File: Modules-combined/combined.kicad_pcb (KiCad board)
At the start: 2 copper layers, 100 x 100 mm, 245 parts

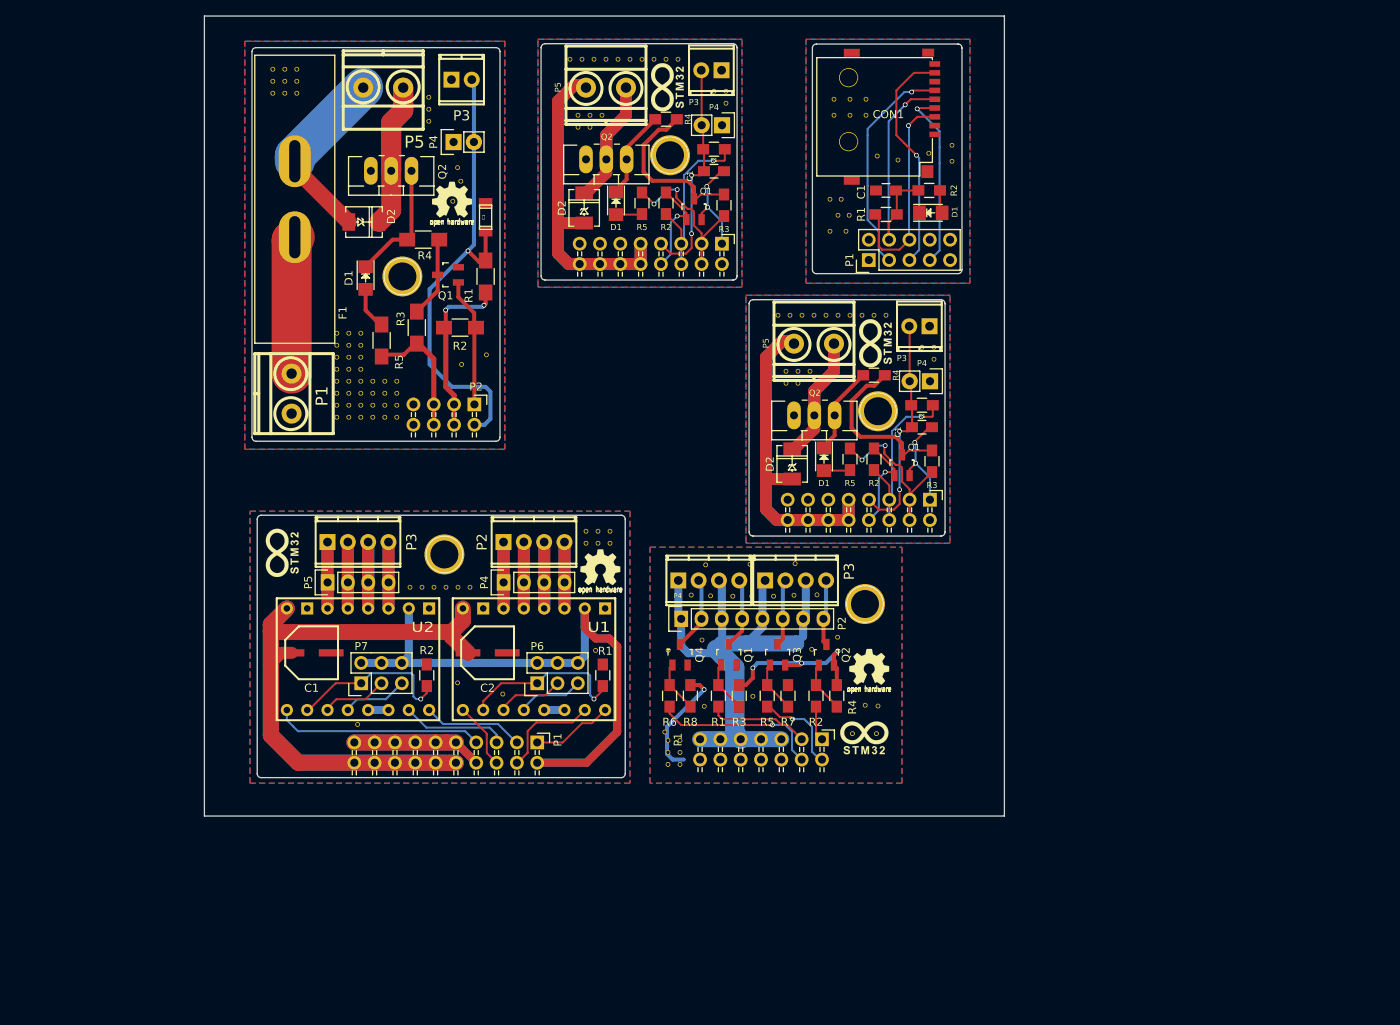
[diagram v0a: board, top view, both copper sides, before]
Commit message: Finished Combined PCB and Gerber files
Combined pcb fits on 10x10cm, breakable and gerbers are finished for elecrow order. will order everything this weekend, lets see if it works.
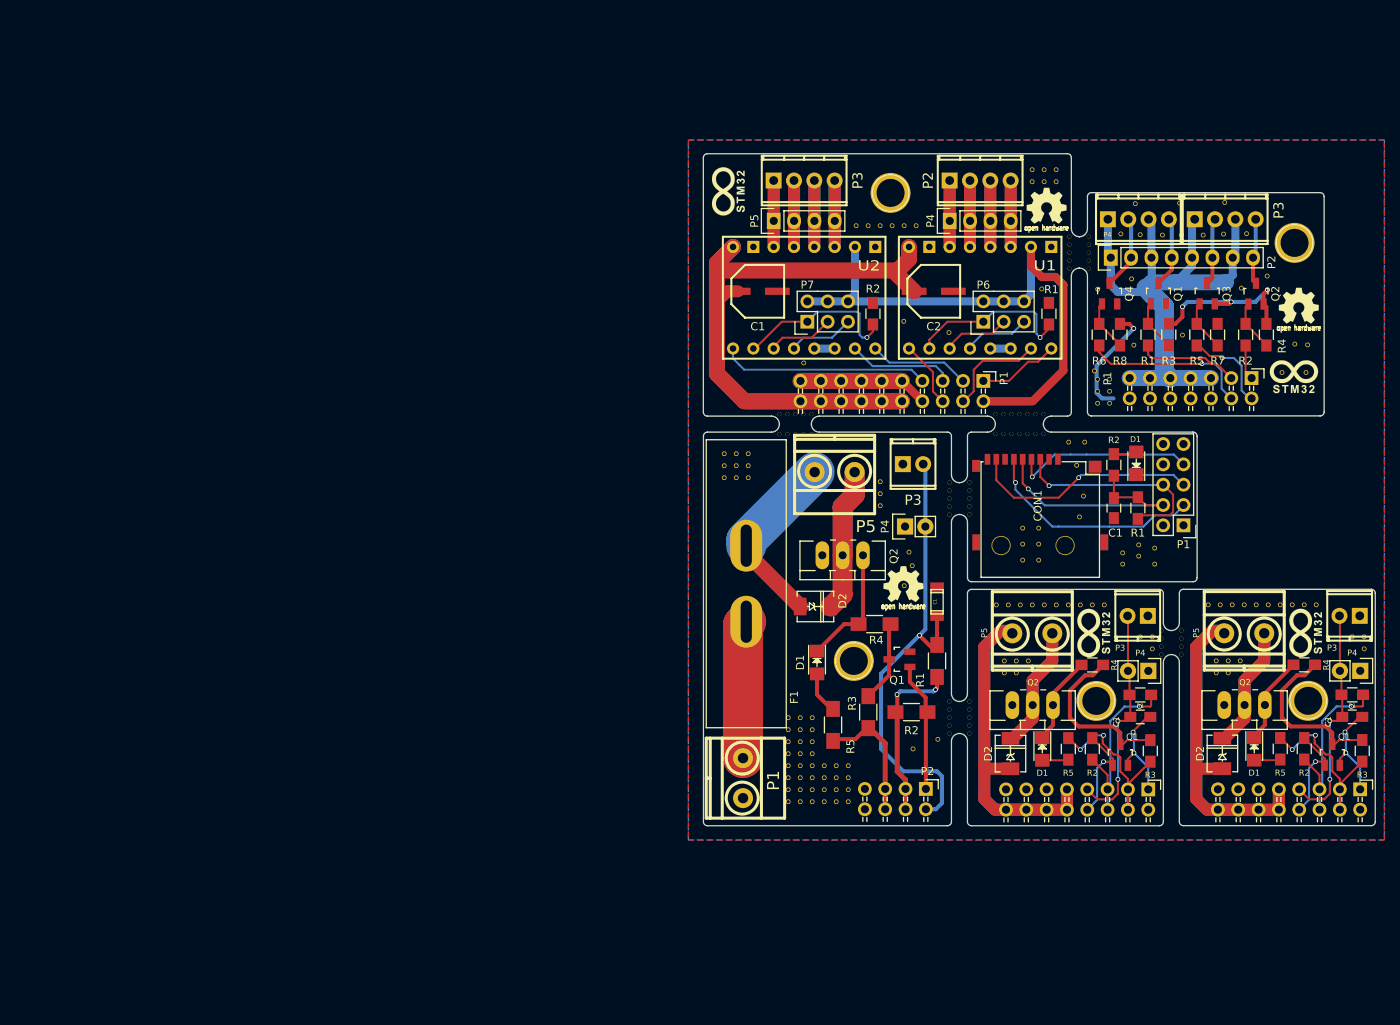
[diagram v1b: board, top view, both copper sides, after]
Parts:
- removed the ? at (189.0, 67.5)
- removed the ? at (189.0, 66.0)
- removed the ? at (187.5, 66.0)
- removed the ? at (172.0, 70.5)
- removed the ? at (170.5, 70.5)
- removed the ? at (173.5, 69.0)
- removed the ? at (172.0, 69.0)
- removed the ? at (170.5, 69.0)
- removed the ? at (183.0, 62.0)
- removed the ? at (181.5, 62.0)
- removed the ? at (180.0, 62.0)
- removed the ? at (178.5, 62.0)
- removed the ? at (177.0, 62.0)
- removed the ? at (175.5, 62.0)
- removed the ? at (174.0, 62.0)
- removed the ? at (172.5, 62.0)
- removed the ? at (171.0, 62.0)
- removed the ? at (181.4, 67.7)
- removed the ? at (181.8, 65.5)
- removed the ? at (182.0, 74.0)
- removed the ? at (169.5, 62.0)
- removed the ? at (146.0, 38.5)
- removed the ? at (144.5, 38.5)
- removed the ? at (147.5, 37.0)
- removed the ? at (146.0, 37.0)
- removed the ? at (144.5, 37.0)
- removed the ? at (151.0, 30.0)
- removed the ? at (149.5, 30.0)
- removed the ? at (148.0, 30.0)
- removed the ? at (146.5, 30.0)
- removed the ? at (145.0, 30.0)
- removed the ? at (143.5, 30.0)
- removed the ? at (163.0, 35.5)
- removed the ? at (163.0, 34.0)
- removed the ? at (161.5, 34.0)
- removed the ? at (157.0, 30.0)
- removed the ? at (155.5, 30.0)
- removed the ? at (154.0, 30.0)
- removed the ? at (152.5, 30.0)
- removed the ? at (155.4, 35.7)
- removed the ? at (155.8, 33.5)
- removed the ? at (156.0, 42.0)
- removed the C1 at (161.5, 44.0)
- removed the C1 at (187.5, 76.0)
- removed the D1 at (149.2, 48.0)
- removed the D1 at (175.2, 80.0)
- removed the D2 at (145.3, 48.6)
- removed the D2 at (171.3, 80.6)
- removed the P1 at (162.5, 53.1)
- removed the P1 at (188.5, 85.1)
- removed the P3 at (161.2, 31.4)
- removed the P3 at (187.2, 63.4)
- removed the P4 at (162.5, 38.2)
- removed the P4 at (188.5, 70.2)
- removed the P5 at (148.0, 33.5)
- removed the P5 at (174.0, 65.5)
- removed the Q1 at (159.0, 48.8)
- removed the Q1 at (185.0, 80.8)
- removed the Q2 at (148.0, 42.5)
- removed the Q2 at (174.0, 74.5)
- removed the R1 at (161.5, 41.2)
- removed the R1 at (187.5, 73.2)
- removed the R2 at (155.5, 48.0)
- removed the R2 at (181.5, 80.0)
- removed the R3 at (162.8, 48.2)
- removed the R3 at (188.8, 80.2)
- removed the R4 at (155.5, 37.5)
- removed the R4 at (181.5, 69.5)
- removed the R5 at (152.5, 48.0)
- removed the R5 at (178.5, 80.0)
- added ?: , ReST-Library:VIA-0.6mm, F.Cu at (202.8, 98.2)
- added ?: , ReST-Library:VIA-0.6mm, F.Cu at (201.3, 98.2)
- added ?: , ReST-Library:VIA-0.6mm, F.Cu at (199.8, 98.2)
- added ?: , ReST-Library:VIA-0.6mm, F.Cu at (198.3, 98.2)
- added ?: , ReST-Library:Logo_silk_OSHW_6x6mm, B.Cu at (208.7, 103.9)
- added ?: , ReST-Library:STM32, F.Cu at (209.0, 101.7)
- added ?: , Connect:1pin, F.Cu at (209.3, 110.2)
- added ?: , ReST-Library:VIA-0.6mm, F.Cu at (196.8, 98.2)
- added ?: , ReST-Library:VIA-0.6mm, F.Cu at (242.8, 103.7)
- added ?: , ReST-Library:VIA-0.6mm, F.Cu at (242.8, 102.2)
- added ?: , ReST-Library:VIA-0.6mm, F.Cu at (241.3, 102.2)
- added ?: , ReST-Library:VIA-0.6mm, F.Cu at (225.8, 106.7)
- added ?: , ReST-Library:VIA-0.6mm, F.Cu at (224.3, 106.7)
- added ?: , ReST-Library:VIA-0.6mm, F.Cu at (227.3, 105.2)
- added ?: , ReST-Library:VIA-0.6mm, F.Cu at (225.8, 105.2)
- added ?: , ReST-Library:VIA-0.6mm, F.Cu at (224.3, 105.2)
- added ?: , ReST-Library:VIA-0.6mm, F.Cu at (236.8, 98.2)
- added ?: , ReST-Library:VIA-0.6mm, F.Cu at (235.3, 98.2)
- added ?: , ReST-Library:VIA-0.6mm, F.Cu at (233.8, 98.2)
- added ?: , ReST-Library:VIA-0.6mm, F.Cu at (232.3, 98.2)
- added ?: , ReST-Library:VIA-0.6mm, F.Cu at (230.8, 98.2)
- added ?: , ReST-Library:VIA-0.6mm, F.Cu at (229.3, 98.2)
- added ?: , ReST-Library:VIA-0.6mm, F.Cu at (227.8, 98.2)
- added ?: , ReST-Library:VIA-0.6mm, F.Cu at (226.3, 98.2)
- added ?: , ReST-Library:VIA-0.6mm, F.Cu at (224.8, 98.2)
- added ?: , ReST-Library:Logo_silk_OSHW_6x6mm, B.Cu at (235.2, 103.9)
- added ?: , ReST-Library:STM32, F.Cu at (235.5, 101.7)
- added ?: , Connect:1pin, F.Cu at (235.8, 110.2)
- added ?: , ReST-Library:VIA-0.6mm, F.Cu at (223.3, 98.2)
- added ?: , ReST-Library:VIA-0.6mm, F.Cu at (216.3, 103.7)
- added ?: , ReST-Library:VIA-0.6mm, F.Cu at (216.3, 102.2)
- added ?: , ReST-Library:VIA-0.6mm, F.Cu at (214.8, 102.2)
- added ?: , ReST-Library:VIA-0.6mm, F.Cu at (199.3, 106.7)
- added ?: , ReST-Library:VIA-0.6mm, F.Cu at (197.8, 106.7)
- added ?: , ReST-Library:VIA-0.6mm, F.Cu at (200.8, 105.2)
- added ?: , ReST-Library:VIA-0.6mm, F.Cu at (199.3, 105.2)
- added ?: , ReST-Library:VIA-0.6mm, F.Cu at (197.8, 105.2)
- added ?: , ReST-Library:VIA-0.6mm, F.Cu at (210.3, 98.2)
- added ?: , ReST-Library:VIA-0.6mm, F.Cu at (208.8, 98.2)
- added ?: , ReST-Library:VIA-0.6mm, F.Cu at (207.3, 98.2)
- added ?: , ReST-Library:VIA-0.6mm, F.Cu at (205.8, 98.2)
- added ?: , ReST-Library:VIA-0.6mm, F.Cu at (204.3, 98.2)
- added C1: , Capacitors_SMD:C_0805_HandSoldering, F.Cu at (214.8, 112.2)
- added C1: , Capacitors_SMD:C_0805_HandSoldering, F.Cu at (241.3, 112.2)
- added D1: , LEDs:LED_1206, F.Cu at (202.5, 116.2)
- added D1: , LEDs:LED_1206, F.Cu at (229.0, 116.2)
- added D2: , ReST-Library:DO-214AC(SMA), F.Cu at (198.6, 116.8)
- added D2: , ReST-Library:DO-214AC(SMA), F.Cu at (225.1, 116.8)
- added P1: , ReST-Library:Pin_Header_Angled_2x08, F.Cu at (215.8, 121.3)
- added P1: , ReST-Library:Pin_Header_Angled_2x08, F.Cu at (242.3, 121.3)
- added P3: , ReST-Library:screw-2,54-2P, F.Cu at (214.5, 99.6)
- added P3: , ReST-Library:screw-2,54-2P, F.Cu at (241.0, 99.6)
- added P4: , Pin_Headers:Pin_Header_Straight_1x02, F.Cu at (215.8, 106.5)
- added P4: , Pin_Headers:Pin_Header_Straight_1x02, F.Cu at (242.3, 106.5)
- added P5: , ReST-Library:screw-5-2P, F.Cu at (201.3, 101.8)
- added P5: , ReST-Library:screw-5-2P, F.Cu at (227.8, 101.8)
- added Q1: , ReST-Library:SOT-23, F.Cu at (212.3, 117.0)
- added Q1: , ReST-Library:SOT-23, F.Cu at (238.8, 117.0)
- added Q2: , TO_SOT_Packages_THT:TO-220_Neutral123_Vertical_LargePads, F.Cu at (201.3, 110.7)
- added Q2: , TO_SOT_Packages_THT:TO-220_Neutral123_Vertical_LargePads, F.Cu at (227.8, 110.7)
- added R1: , Resistors_SMD:R_0805_HandSoldering, F.Cu at (214.8, 109.5)
- added R1: , Resistors_SMD:R_0805_HandSoldering, F.Cu at (241.3, 109.5)
- added R2: , Resistors_SMD:R_0805_HandSoldering, F.Cu at (208.8, 116.2)
- added R2: , Resistors_SMD:R_0805_HandSoldering, F.Cu at (235.3, 116.2)
- added R3: , Resistors_SMD:R_0805_HandSoldering, F.Cu at (216.0, 116.5)
- added R3: , Resistors_SMD:R_0805_HandSoldering, F.Cu at (242.5, 116.5)
- added R4: , Resistors_SMD:R_0805_HandSoldering, F.Cu at (208.8, 105.7)
- added R4: , Resistors_SMD:R_0805_HandSoldering, F.Cu at (235.3, 105.7)
- added R5: , Resistors_SMD:R_0805_HandSoldering, F.Cu at (205.8, 116.2)
- added R5: , Resistors_SMD:R_0805_HandSoldering, F.Cu at (232.3, 116.2)
- added REF**11: , ReST-Library:VIA-0.6mm, F.Cu at (169.7, 74.4)
- added REF**111: , ReST-Library:VIA-0.6mm, F.Cu at (169.7, 76.9)
- added REF**11111: , ReST-Library:VIA-0.6mm, F.Cu at (196.7, 74.4)
- added REF**111111: , ReST-Library:VIA-0.6mm, F.Cu at (190.9, 82.9)
- added REF**111111: , ReST-Library:VIA-0.6mm, F.Cu at (196.7, 76.8)
- added REF**11111111: , ReST-Library:VIA-0.6mm, F.Cu at (205.9, 52.2)
- added REF**111111111: , ReST-Library:VIA-0.6mm, F.Cu at (193.4, 82.9)
- added REF**111111111: , ReST-Library:VIA-0.6mm, F.Cu at (208.3, 52.2)
- added REF**1111111111: , ReST-Library:VIA-0.6mm, F.Cu at (190.9, 110.3)
- added REF**11111111111: , ReST-Library:VIA-0.6mm, F.Cu at (193.4, 110.3)
- added REF**1111111111111: , ReST-Library:VIA-0.6mm, F.Cu at (217.4, 101.4)
- added REF**11111111111111: , ReST-Library:VIA-0.6mm, F.Cu at (219.9, 101.4)
- added REF**11111111111112: , ReST-Library:VIA-0.6mm, F.Cu at (219.9, 102.4)
- added REF**11111111111113: , ReST-Library:VIA-0.6mm, F.Cu at (219.9, 103.4)
- added REF**11111111111114: , ReST-Library:VIA-0.6mm, F.Cu at (219.9, 104.4)
- added REF**1111111111112: , ReST-Library:VIA-0.6mm, F.Cu at (217.4, 102.4)
- added REF**1111111111113: , ReST-Library:VIA-0.6mm, F.Cu at (217.4, 103.4)
- added REF**1111111111114: , ReST-Library:VIA-0.6mm, F.Cu at (217.4, 104.4)
- added REF**11111111112: , ReST-Library:VIA-0.6mm, F.Cu at (193.4, 111.3)
- added REF**11111111113: , ReST-Library:VIA-0.6mm, F.Cu at (193.4, 112.3)
- added REF**11111111114: , ReST-Library:VIA-0.6mm, F.Cu at (193.4, 113.3)
- added REF**11111111115: , ReST-Library:VIA-0.6mm, F.Cu at (193.4, 114.3)
- added REF**1111111112: , ReST-Library:VIA-0.6mm, F.Cu at (190.9, 111.3)
- added REF**1111111113: , ReST-Library:VIA-0.6mm, F.Cu at (190.9, 112.3)
- added REF**1111111114: , ReST-Library:VIA-0.6mm, F.Cu at (190.9, 113.3)
- added REF**1111111115: , ReST-Library:VIA-0.6mm, F.Cu at (190.9, 114.3)
- added REF**111111112: , ReST-Library:VIA-0.6mm, F.Cu at (193.4, 83.9)
- added REF**111111112: , ReST-Library:VIA-0.6mm, F.Cu at (208.3, 53.2)
- added REF**111111113: , ReST-Library:VIA-0.6mm, F.Cu at (193.4, 84.9)
- added REF**111111113: , ReST-Library:VIA-0.6mm, F.Cu at (208.3, 54.2)
- added REF**111111114: , ReST-Library:VIA-0.6mm, F.Cu at (193.4, 85.9)
- added REF**111111114: , ReST-Library:VIA-0.6mm, F.Cu at (208.3, 55.2)
- added REF**111111115: , ReST-Library:VIA-0.6mm, F.Cu at (193.4, 86.9)
- added REF**111111115: , ReST-Library:VIA-0.6mm, F.Cu at (208.3, 56.2)
- added REF**11111112: , ReST-Library:VIA-0.6mm, F.Cu at (205.9, 53.2)
- added REF**11111113: , ReST-Library:VIA-0.6mm, F.Cu at (205.9, 54.2)
- added REF**11111114: , ReST-Library:VIA-0.6mm, F.Cu at (205.9, 55.2)
- added REF**11111115: , ReST-Library:VIA-0.6mm, F.Cu at (205.9, 56.2)
- added REF**111112: , ReST-Library:VIA-0.6mm, F.Cu at (190.9, 83.9)
- added REF**111113: , ReST-Library:VIA-0.6mm, F.Cu at (190.9, 84.9)
- added REF**111114: , ReST-Library:VIA-0.6mm, F.Cu at (190.9, 85.9)
- added REF**111115: , ReST-Library:VIA-0.6mm, F.Cu at (190.9, 86.9)
- added REF**111121: , ReST-Library:VIA-0.6mm, F.Cu at (197.7, 76.8)
- added REF**111131: , ReST-Library:VIA-0.6mm, F.Cu at (198.7, 76.8)
- added REF**111141: , ReST-Library:VIA-0.6mm, F.Cu at (199.7, 76.8)
- added REF**111151: , ReST-Library:VIA-0.6mm, F.Cu at (200.7, 76.8)
- added REF**111161: , ReST-Library:VIA-0.6mm, F.Cu at (201.7, 76.8)
- added REF**111171: , ReST-Library:VIA-0.6mm, F.Cu at (202.7, 76.8)
- added REF**11121: , ReST-Library:VIA-0.6mm, F.Cu at (197.7, 74.4)
- added REF**11131: , ReST-Library:VIA-0.6mm, F.Cu at (198.7, 74.4)
- added REF**11141: , ReST-Library:VIA-0.6mm, F.Cu at (199.7, 74.4)
- added REF**11151: , ReST-Library:VIA-0.6mm, F.Cu at (200.7, 74.4)
- added REF**11161: , ReST-Library:VIA-0.6mm, F.Cu at (201.7, 74.4)
- added REF**11171: , ReST-Library:VIA-0.6mm, F.Cu at (202.7, 74.4)
- added REF**121: , ReST-Library:VIA-0.6mm, F.Cu at (170.7, 76.9)
- added REF**131: , ReST-Library:VIA-0.6mm, F.Cu at (171.7, 76.9)
- added REF**141: , ReST-Library:VIA-0.6mm, F.Cu at (172.7, 76.9)
- added REF**151: , ReST-Library:VIA-0.6mm, F.Cu at (173.7, 76.9)
- added REF**21: , ReST-Library:VIA-0.6mm, F.Cu at (170.7, 74.4)
- added REF**31: , ReST-Library:VIA-0.6mm, F.Cu at (171.7, 74.4)
- added REF**41: , ReST-Library:VIA-0.6mm, F.Cu at (172.7, 74.4)
- added REF**51: , ReST-Library:VIA-0.6mm, F.Cu at (173.7, 74.4)
- moved ? 74.1 mm to (186.4, 116.2)
- moved ? 74.1 mm to (189.5, 115.0)
- moved ? 74.1 mm to (178.3, 122.8)
- moved ? 74.1 mm to (176.8, 122.8)
- moved ? 74.1 mm to (175.3, 122.8)
- moved ? 74.1 mm to (178.3, 121.3)
- moved ? 74.1 mm to (176.8, 121.3)
- moved ? 74.1 mm to (175.3, 121.3)
- moved ? 74.1 mm to (178.3, 119.8)
- moved ? 74.1 mm to (176.8, 119.8)
- moved ? 74.1 mm to (175.3, 119.8)
- moved ? 74.1 mm to (178.3, 118.3)
- moved ? 74.1 mm to (176.8, 118.3)
- moved ? 74.1 mm to (175.3, 118.3)
- moved ? 74.1 mm to (185.3, 95.8)
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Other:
- board size 100 x 100 mm -> 84 x 84 mm
- rule pad_to_mask_clearance: 0 -> 0.2

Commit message: minor changes to values of components and footprints. added two leds for both 12V Rails.
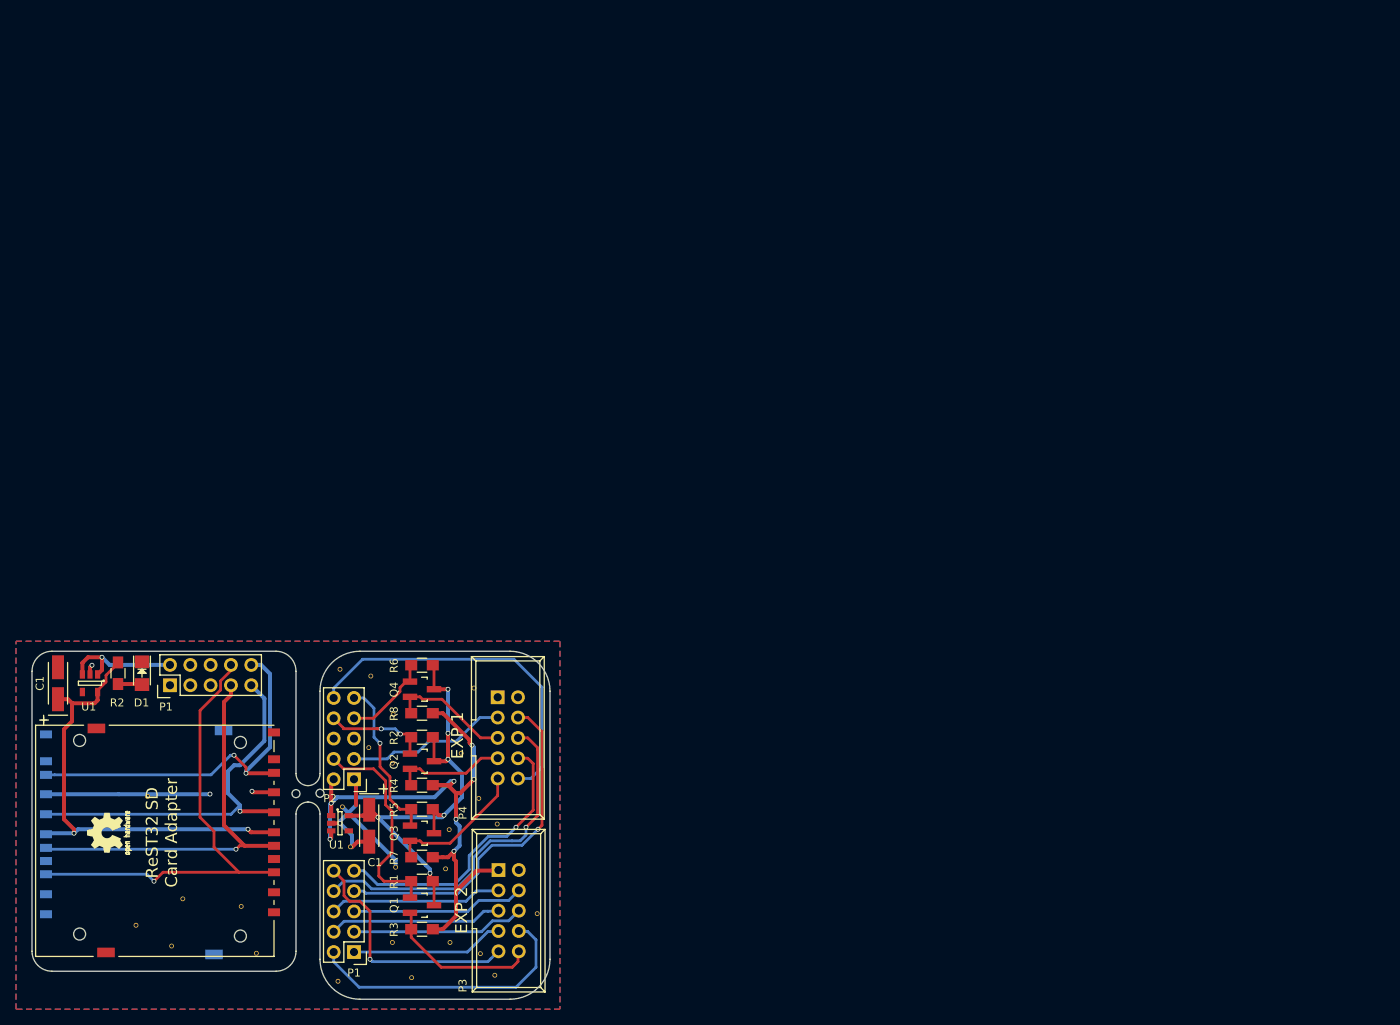
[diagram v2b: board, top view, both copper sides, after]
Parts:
- removed ? (x149), REF**11, REF**111, REF**11111, REF**111111 (x2), REF**11111111, REF**111111111 (x2), REF**1111111111, REF**11111111111, REF**1111111111111, REF**11111111111111, REF**11111111111112, REF**11111111111113, REF**11111111111114, REF**1111111111112, REF**1111111111113, REF**1111111111114, REF**11111111112, REF**11111111113, REF**11111111114, REF**11111111115, REF**1111111112, REF**1111111113, REF**1111111114, REF**1111111115, REF**111111112 (x2), REF**111111113 (x2), REF**111111114 (x2), REF**111111115 (x2), REF**11111112, REF**11111113, REF**11111114, REF**11111115, REF**111112, REF**111113, REF**111114, REF**111115, REF**111121, REF**111131, REF**111141, REF**111151, REF**111161, REF**111171, REF**11121, REF**11131, REF**11141, REF**11151, REF**11161, REF**11171, REF**121, REF**131, REF**141, REF**151, REF**21, REF**31, REF**41, REF**51: , ReST-Library:VIA-0.6mm
- removed ? (x6): , ReST-Library:Logo_silk_OSHW_6x6mm
- removed ? (x4): , ReST-Library:STM32
- removed ? (x5): , Connect:1pin
- removed ? (x2): , ReST-Library:STM32-6mm
- removed the C1 at (189.4, 97.8)
- removed the C1 at (214.8, 112.2)
- removed the C1 at (211.5, 86.1)
- removed the C1 at (241.3, 112.2)
- removed the C1 at (167.0, 59.0)
- removed C2: , ReST-Library:CP-PANASONIC-SMT_D8
- removed the D1 at (174.4, 105.4)
- removed the D1 at (202.5, 116.2)
- removed the D1 at (214.3, 80.5)
- removed the D1 at (229.0, 116.2)
- removed D2: , DO-214AC(SMA):DO-214AC(SMA)
- removed D2 (x2): , ReST-Library:DO-214AC(SMA)
- removed F1: , ReST-Librar:JEF-703C
- removed the P1 at (228.7, 69.9)
- removed the P1 at (165.1, 119.9)
- removed the P1 at (215.8, 121.3)
- removed the P1 at (220.2, 88.3)
- removed the P1 at (242.3, 121.3)
- removed the P1 at (195.2, 70.2)
- removed the P2 at (211.1, 54.8)
- removed the P2 at (188.0, 121.2)
- removed the P2 at (194.8, 45.2)
- removed the P3 at (225.4, 50.0)
- removed the P3 at (186.4, 80.6)
- removed the P3 at (214.5, 99.6)
- removed the P3 at (241.0, 99.6)
- removed the P3 at (172.8, 45.2)
- removed the P4 at (214.6, 50.0)
- removed the P4 at (185.4, 88.4)
- removed the P4 at (215.8, 106.5)
- removed the P4 at (242.3, 106.5)
- removed the P4 at (191.0, 50.2)
- removed P5: , 5mm-pitch-terminal:mkds_1,5-2
- removed P5 (x2): , ReST-Library:screw-5-2P
- removed P5: , Pin_Headers:Pin_Header_Straight_1x04
- removed P6, P7: , Pin_Headers:Pin_Header_Straight_2x03
- removed the Q1 at (217.1, 59.3)
- removed the Q1 at (184.7, 105.0)
- removed the Q1 at (212.3, 117.0)
- removed the Q1 at (238.8, 117.0)
- removed the Q2 at (229.2, 59.3)
- removed the Q2 at (177.6, 92.0)
- removed the Q2 at (201.3, 110.7)
- removed the Q2 at (227.8, 110.7)
- removed the R1 at (215.8, 64.4)
- removed the R1 at (189.4, 105.2)
- removed the R1 at (214.8, 109.5)
- removed the R1 at (214.5, 86.1)
- removed the R1 at (241.3, 109.5)
- removed the R1 at (203.4, 61.8)
- removed the R2 at (227.9, 64.4)
- removed the R2 at (186.2, 111.6)
- removed the R2 at (208.8, 116.2)
- removed the R2 at (211.5, 80.7)
- removed the R2 at (235.3, 116.2)
- removed the R2 at (181.4, 61.8)
- removed the R3 at (218.3, 64.4)
- removed the R3 at (180.8, 111.6)
- removed the R3 at (216.0, 116.5)
- removed the R3 at (242.5, 116.5)
- removed the R4 at (230.6, 64.4)
- removed the R4 at (181.6, 100.6)
- removed the R4 at (208.8, 105.7)
- removed the R4 at (235.3, 105.7)
- removed the R5 at (221.8, 64.4)
- removed the R5 at (176.4, 113.2)
- removed the R5 at (205.8, 116.2)
- removed the R5 at (232.3, 116.2)
- removed the U1 at (194.8, 59.8)
- removed U2: , ReST-Library:SWDIP8_.6W
- added C1: 2.2uF, Capacitors_Tantalum_SMD:TantalC_SizeA_EIA-3216_HandSoldering, F.Cu at (118.4, 125.8)
- added C1: CP1_Small, Capacitors_Tantalum_SMD:TantalC_SizeA_EIA-3216_HandSoldering, F.Cu at (79.5, 108.0)
- added CON2: uSD_Card, Connect:SD_Card_Receptacle, B.Cu at (78.0, 127.5)
- added D1: Led_Small, LEDs:LED_1206, F.Cu at (90.0, 106.8)
- added G***: LOGO, ReST-Library:Logo_silk_OSHW_6x6mm, B.Cu at (115.5, 125.5)
- added G***: LOGO, ReST-Library:Logo_silk_OSHW_6x6mm, B.Cu at (85.4, 126.7)
- added G***: LOGO, ReST-Library:Logo_silk_OSHW_6x6mm, F.Cu at (85.4, 126.7)
- added P1: CONN_02X05, Pin_Headers:Pin_Header_Straight_2x05, F.Cu at (116.5, 141.6)
- added P1: CONN_02X05, Pin_Headers:Pin_Header_Straight_2x05, F.Cu at (93.5, 108.2)
- added P2: CONN_02X05, Pin_Headers:Pin_Header_Straight_2x05, F.Cu at (116.5, 120.0)
- added P3: CONN_02X05, Connect:IDC_Header_Straight_10pins, F.Cu at (134.6, 131.3)
- added P4: CONN_02X05, Connect:IDC_Header_Straight_10pins, F.Cu at (134.5, 109.8)
- added Q1: BSS138, TO_SOT_Packages_SMD:SOT-23_Handsoldering, F.Cu at (125.0, 135.8)
- added Q2: BSS138, TO_SOT_Packages_SMD:SOT-23_Handsoldering, F.Cu at (125.0, 117.8)
- added R1: 10K, Resistors_SMD:R_0805_HandSoldering, F.Cu at (125.0, 132.8)
- added R2: 10K, Resistors_SMD:R_0805_HandSoldering, F.Cu at (125.0, 114.8)
- added R2: 1K, Resistors_SMD:R_0805_HandSoldering, F.Cu at (87.0, 106.8)
- added R3: 10K, Resistors_SMD:R_0805_HandSoldering, F.Cu at (125.0, 138.8)
- added R4: 10K, Resistors_SMD:R_0805_HandSoldering, F.Cu at (125.0, 120.8)
- added R5: 10K, Resistors_SMD:R_0805_HandSoldering, F.Cu at (125.0, 123.8)
- added REF**: 1pin, ReST-Library:1pin, F.Cu at (112.2, 121.8)
- added REF**: 1pin, ReST-Library:1pin, F.Cu at (121.7, 131.0)
- added REF**: 1pin, ReST-Library:1pin, F.Cu at (121.3, 118.0)
- added REF**: 1pin, ReST-Library:1pin, F.Cu at (114.5, 145.2)
- added REF**: 1pin, ReST-Library:1pin, F.Cu at (114.8, 106.2)
- added REF**: 1pin, ReST-Library:1pin, F.Cu at (118.6, 107.1)
- added REF**: 1pin, ReST-Library:1pin, F.Cu at (131.5, 108.6)
- added REF**: 1pin, ReST-Library:1pin, F.Cu at (132.1, 122.4)
- added REF**: 1pin, ReST-Library:1pin, F.Cu at (134.4, 125.6)
- added REF**: 1pin, ReST-Library:1pin, F.Cu at (139.4, 136.8)
- added REF**: 1pin, ReST-Library:1pin, F.Cu at (134.1, 144.5)
- added REF**: 1pin, ReST-Library:1pin, F.Cu at (109.2, 121.8)
- added REF**: 1pin, ReST-Library:1pin, F.Cu at (132.3, 141.8)
- added REF**: 1pin, ReST-Library:1pin, F.Cu at (128.5, 140.4)
- added REF**: 1pin, ReST-Library:1pin, F.Cu at (121.3, 140.4)
- added REF**: 1pin, ReST-Library:1pin, F.Cu at (123.7, 144.8)
- added REF**: 1pin, ReST-Library:1pin, F.Cu at (95.1, 134.9)
- added REF**: 1pin, ReST-Library:1pin, F.Cu at (89.2, 138.2)
- added REF**: 1pin, ReST-Library:1pin, F.Cu at (102.4, 135.9)
- added REF**: 1pin, ReST-Library:1pin, F.Cu at (104.3, 141.8)
- added REF**: 1pin, ReST-Library:1pin, F.Cu at (90.7, 122.2)
- added REF**: 1pin, ReST-Library:1pin, F.Cu at (93.7, 140.8)
- added REF**: 1pin, ReST-Library:1pin, F.Cu at (118.3, 116.0)
- added REF**: 1pin, ReST-Library:1pin, F.Cu at (121.4, 111.9)
- added REF**: 1pin, ReST-Library:1pin, F.Cu at (129.9, 116.8)
- added REF**: 1pin, ReST-Library:1pin, F.Cu at (128.0, 131.2)
- added REF**: 1pin, ReST-Library:1pin, F.Cu at (116.0, 128.4)
- added REF**: 1pin, ReST-Library:1pin, F.Cu at (115.0, 123.5)
- added REF**: 1pin, ReST-Library:1pin, F.Cu at (128.4, 126.3)
- added U1: MIC5205, TO_SOT_Packages_SMD:SOT-23-5, F.Cu at (114.8, 125.5)
- added U1: MIC5205, TO_SOT_Packages_SMD:SOT-23-5, F.Cu at (83.5, 108.0)
- CON1: value (none) -> uSD_Card; footprint ReST-Library:uSD -> Connect:SD_Card_Receptacle
- Q3, Q4: value (none) -> BSS138; footprint ReST-Library:SOT-23 -> TO_SOT_Packages_SMD:SOT-23_Handsoldering
- R6, R7, R8: value (none) -> 10K
- moved Q3 119.1 mm to (125.0, 126.8), turned to 270 degrees
- moved R7 119.0 mm to (125.0, 129.8), turned to 180 degrees
- moved CON1 106.7 mm to (106.5, 127.2), turned to 270 degrees
- moved R8 99.3 mm to (125.0, 111.8), turned to 180 degrees
- moved Q4 99.2 mm to (125.0, 108.8), turned to 270 degrees
- moved R6 94.2 mm to (125.0, 105.8), turned to 180 degrees
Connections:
- Q3 pad 1: Net-(Q3-Pad1) -> /SPI_SCK
- Q3 pad 2: GND -> /SCK
- Q3 pad 3: /PWM-OUT2 -> +3V3
- Q4 pad 1: Net-(Q4-Pad1) -> /SPI_MOSI
- Q4 pad 2: GND -> /MOSI
- Q4 pad 3: /PWM-OUT3 -> +3V3
- R6 pad 1: /PWM-ADD3 -> +3V3
- R6 pad 2: Net-(Q4-Pad1) -> /SPI_MOSI
- R7 pad 1: Net-(Q3-Pad1) -> +5V
- R7 pad 2: GND -> /SCK
- R8 pad 1: Net-(Q4-Pad1) -> +5V
- R8 pad 2: GND -> /MOSI
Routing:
- net +12V: track 370.8 -> 0.00 mm
- net +3V3: track 200.1 -> 115.7 mm, vias 5 -> 8
- net Net-(D2-Pad2): track 81.2 -> 0.00 mm
- net /T0: track 60.0 -> 0.00 mm, vias 1 -> 0
- net /T1: track 56.7 -> 0.00 mm, vias 4 -> 0
- net Net-(Q1-Pad3): track 53.8 -> 0.00 mm
- net GND: track 93.5 -> 48.5 mm, vias 8 -> 4
- net /MISO: track 0.00 -> 43.8 mm
- net /DISPLAY_D5: track 0.00 -> 43.6 mm, vias 0 -> 1
- net /DISPLAY_D4: track 0.00 -> 43.2 mm, vias 0 -> 1
- net Net-(D1-Pad1): track 40.0 -> 0.00 mm
- net /DISPLAY_D7: track 0.00 -> 36.0 mm, vias 0 -> 1
- net /DISPLAY_CD: track 0.00 -> 35.0 mm
- net +5V: track 59.0 -> 91.4 mm, vias 4 -> 8
- net /SPI-CS: track 26.9 -> 58.9 mm
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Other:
- board size 84 x 84 mm -> 64.8 x 43.5 mm
- net class Default: trace_width 0.25 -> 0.3
- board text added: "EXP 1"
- board text added: "EXP 2"
- board text added: "ReST32 LCD Adapter for RepRapDiscount Full Graphic Smart Controller"
- board text added: "ReST32 SD Card Adapter"
- board text removed: "@maker_berry"
- board text removed: "Additional Module - IRLML2502 Rev. A @maker_berry"
- board text removed: "ReST SD Card Adapter Rev. A @maker_berry"
- board text removed: "ReST32 Heatbed Module Rev. A | Test"
- board text removed: "ReST32 Heater Rev. A | Test @maker_berry"
- board text removed: "ReST32 Stepper Module Rev. A @maker_berry"

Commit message: final release. PCBs ordered
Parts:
- removed the REF** at (114.8, 106.2)
- D1: footprint LEDs:LED_1206 -> LEDs:LED_0805
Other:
- outline, holes or cut-outs redrawn
